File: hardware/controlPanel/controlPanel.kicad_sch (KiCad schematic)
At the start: 17 parts, among them J1 Power Supply, J2 Conn_01x08_Female, SW1 Ein/Aus, SW2 Fallschirm schließen, U1 LM555xM

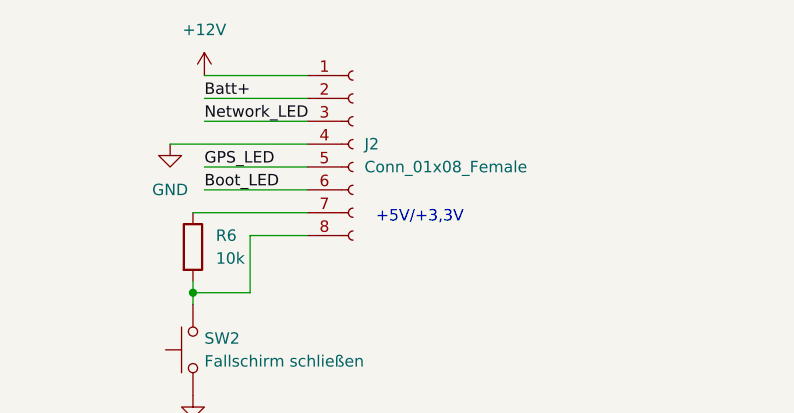
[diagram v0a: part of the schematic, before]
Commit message: changed the footprint of the connector to the controlPanel and changed the order of the pin numbers
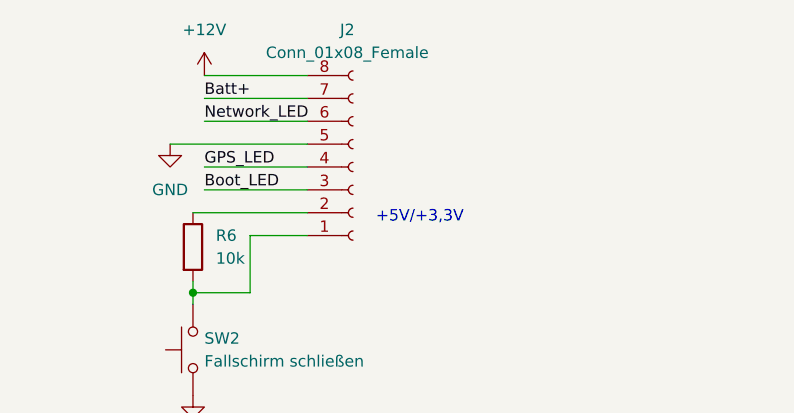
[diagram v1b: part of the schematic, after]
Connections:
- net +12V: now also J2.8 (Pin_8); no longer J2.1 (Pin_1)
- net Batt+: now also J2.7 (Pin_7); no longer J2.2 (Pin_2)
- net Boot_LED: now also J2.3 (Pin_3); no longer J2.6 (Pin_6)
- net GND: now also J2.5 (Pin_5); no longer J2.4 (Pin_4)
- net GPS_LED: now also J2.4 (Pin_4); no longer J2.5 (Pin_5)
- net Network_LED: now also J2.6 (Pin_6); no longer J2.3 (Pin_3)
- net at R6.1: now also J2.2 (Pin_2); no longer J2.7 (Pin_7)
- net at R6.2, SW2.2: now also J2.1 (Pin_1); no longer J2.8 (Pin_8)
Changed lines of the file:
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@@
     (pin "2")
   )
-  (symbol (lib_id "Connector:Conn_01x08_Female") (at 180.34 45.72 0) (unit 1)
+  (symbol (lib_id "Connector:Conn_01x08_Female") (at 180.34 48.26 0) (mirror x) (unit 1)
     (in_bom yes) (on_board yes) (fields_autoplaced)
-    (property "Reference" "J2" (id 0) (at 181.61 45.7199 0)
-      (effects (font (size 1.27 1.27)) (justify left))
-    )
-    (property "Value" "Conn_01x08_Female" (id 1) (at 181.61 48.2599 0)
-      (effects (font (size 1.27 1.27)) (justify left))
-    )
-    (property "Footprint" "Connector_PinHeader_2.00mm:PinHeader_1x08_P2.00mm_Vertical" (id 2) (at 180.34 45.72 0)
+    (property "Reference" "J2" (id 0) (at 179.705 33.02 0))
+    (property "Value" "Conn_01x08_Female" (id 1) (at 179.705 35.56 0))
+    (property "Footprint" "Connector_PinHeader_2.00mm:PinHeader_1x08_P2.00mm_Vertical" (id 2) (at 180.34 48.26 0)
       (effects (font (size 1.27 1.27)) hide)
     )
-    (property "Datasheet" "~" (id 3) (at 180.34 45.72 0)
+    (property "Datasheet" "~" (id 3) (at 180.34 48.26 0)
       (effects (font (size 1.27 1.27)) hide)
     )
